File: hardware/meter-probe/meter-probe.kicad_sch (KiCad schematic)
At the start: 29 parts, among them J1 Cable, J2 Cable, Q1 BSS138, SW1 Sensor Button, U1 RT9193, U2 TCS3472, U3 TCA9517A, U4 USBLC6-2SC6, U5 M24C02-D

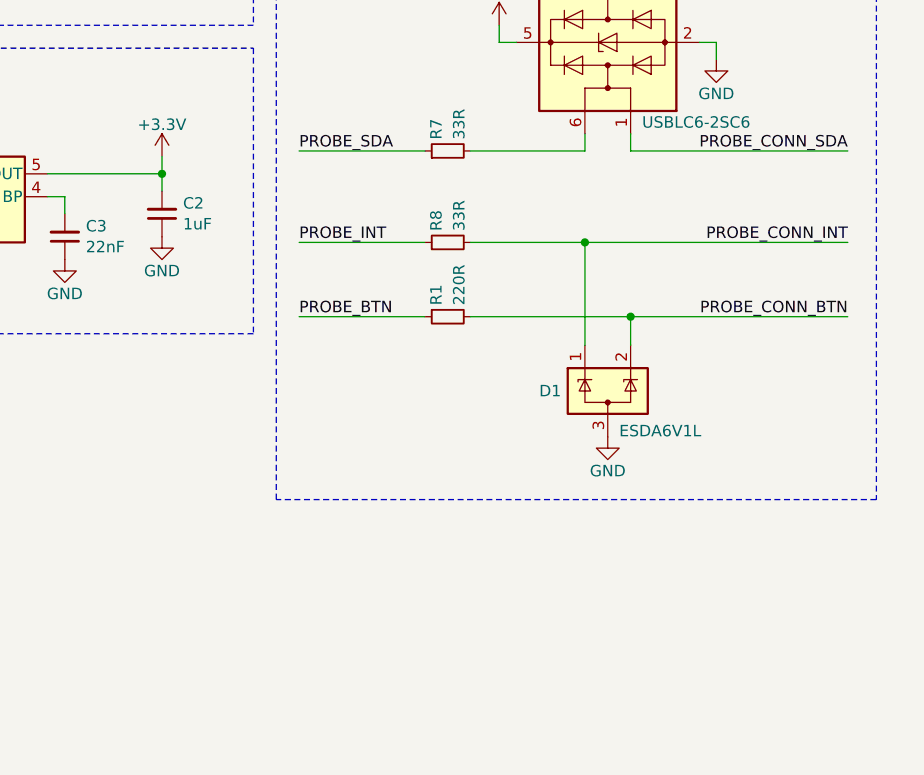
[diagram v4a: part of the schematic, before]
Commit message: Update meter probe PCB layout based on schematic changes
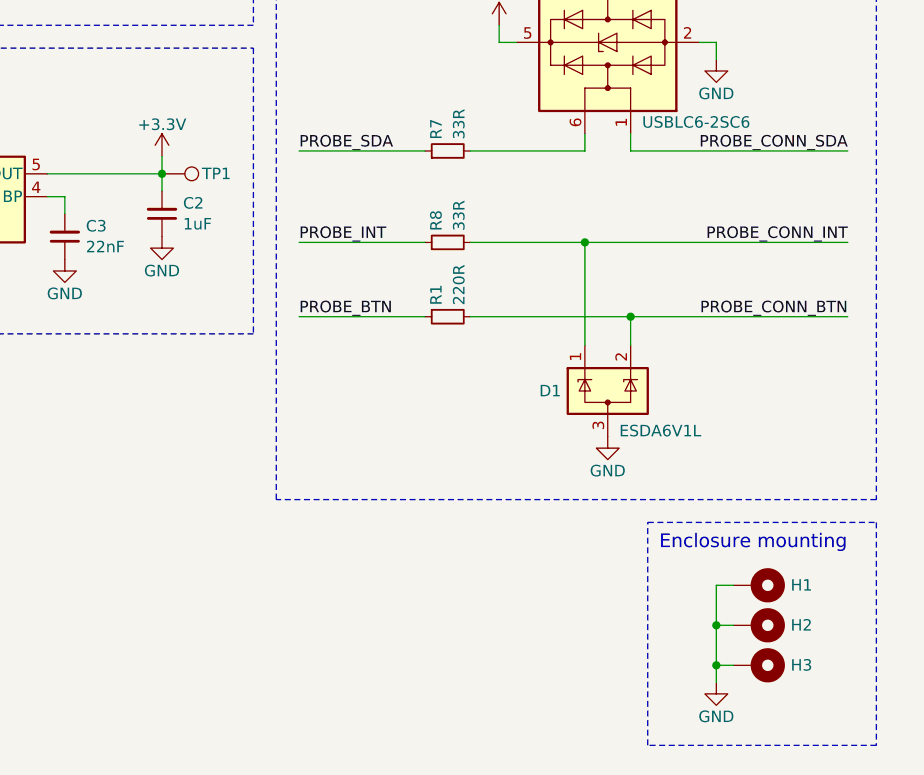
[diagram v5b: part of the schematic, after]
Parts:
- added H1, H2, H3: MountingHole_Pad, MountingHole:MountingHole_2.7mm_M2.5_Pad_Via, symbol Mechanical:MountingHole_Pad
- added TP1: TestPoint, TestPoint:TestPoint_Pad_D2.0mm, symbol Connector:TestPoint
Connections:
- net +3.3V: now also TP1.1
- net GND: now also H1.1, H2.1, H3.1
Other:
- note added: "Enclosure mounting"
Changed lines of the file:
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@@
   (junction (at 125.095 27.305) (diameter 0) (color 0 0 0 0)
   )
+  (junction (at 245.745 148.59) (diameter 0) (color 0 0 0 0)
+  )
   (junction (at 175.26 37.465) (diameter 0) (color 0 0 0 0)
   )
@@
   )
   (junction (at 121.92 41.275) (diameter 0) (color 0 0 0 0)
+  )
+  (junction (at 245.745 153.035) (diameter 0) (color 0 0 0 0)
   )
   (junction (at 168.91 41.275) (diameter 0) (color 0 0 0 0)
@@
     (stroke (width 0) (type default))
   )
+  (wire (pts (xy 245.745 153.035) (xy 245.745 154.94))
+    (stroke (width 0) (type default))
+  )
   (wire (pts (xy 217.805 36.195) (xy 222.885 36.195))
     (stroke (width 0) (type default))
@@
     (stroke (width 0) (type default))
   )
+  (wire (pts (xy 245.745 148.59) (xy 245.745 153.035))
+    (stroke (width 0) (type default))
+  )
   (wire (pts (xy 128.27 27.305) (xy 128.27 28.575))
     (stroke (width 0) (type default))
@@
     (stroke (width 0) (type default))
   )
+  (wire (pts (xy 245.745 153.035) (xy 247.65 153.035))
+    (stroke (width 0) (type default))
+  )
   (wire (pts (xy 199.39 38.735) (xy 222.885 38.735))
     (stroke (width 0) (type default))
@@
     (stroke (width 0) (type default))
   )
+  (wire (pts (xy 245.745 148.59) (xy 247.65 148.59))
+    (stroke (width 0) (type default))
+  )
+  (wire (pts (xy 245.745 144.145) (xy 245.745 148.59))
+    (stroke (width 0) (type default))
+  )
   (wire (pts (xy 125.095 27.305) (xy 128.27 27.305))
     (stroke (width 0) (type default))
@@
   )
   (wire (pts (xy 245.745 83.82) (xy 245.745 85.725))
+    (stroke (width 0) (type default))
+  )
+  (wire (pts (xy 247.65 144.145) (xy 245.745 144.145))
     (stroke (width 0) (type default))
   )
@@
     (fill (type none))
   )
+  (rectangle (start 238.125 137.16) (end 263.525 161.925)
+    (stroke (width 0) (type dash))
+    (fill (type none))
+  )
   (rectangle (start 240.03 17.78) (end 261.62 38.1)
     (stroke (width 0) (type default))
@@
     (at 104.14 80.645 0)
     (effects (font (size 1.27 1.27)) (justify left bottom))
+  )
+  (text "Enclosure mounting" (at 239.395 140.335 0)
+    (effects (font (size 1.524 1.524)) (justify left bottom))
   )
   (text "Red" (at 254 26.67 0)
@@
         (path "/1f1005f7-3f58-4453-9bfa-bdc1c0b6f7ed"
           (reference "#PWR0119") (unit 1)
+        )
+      )
+    )
+  )
+  (symbol (lib_id "Mechanical:MountingHole_Pad") (at 250.19 144.145 270) (unit 1)
+    (in_bom no) (on_board yes) (dnp no)
+    (property "Reference" "H1" (at 254 144.145 90)
+      (effects (font (size 1.27 1.27)) (justify left))
+    )
+    (property "Value" "MountingHole_Pad" (at 254 146.05 90)
+      (effects (font (size 1.27 1.27)) (justify left) hide)
+    )
+    (property "Footprint" "MountingHole:MountingHole_2.7mm_M2.5_Pad_Via" (at 250.19 144.145 0)
+      (effects (font (size 1.27 1.27)) hide)
+    )
+    (property "Datasheet" "~" (at 250.19 144.145 0)
+      (effects (font (size 1.27 1.27)) hide)
+    )
+    (property "Description" "" (at 250.19 144.145 0)
+      (effects (font (size 1.27 1.27)) hide)
+    )
+    (property "Manufacturer" "" (at 250.19 144.145 0)
+      (effects (font (size 1.27 1.27)) hide)
+    )
+    (property "Manufacturer PN" "" (at 250.19 144.145 0)
+      (effects (font (size 1.27 1.27)) hide)
+    )
+    (property "Supplier" "" (at 250.19 144.145 0)
+      (effects (font (size 1.27 1.27)) hide)
+    )
+    (property "Supplier PN" "" (at 250.19 144.145 0)
+      (effects (font (size 1.27 1.27)) hide)
+    )
+    (pin "1")
+    (instances
+      (project "meter-probe"
+        (path "/1f1005f7-3f58-4453-9bfa-bdc1c0b6f7ed"
+          (reference "H1") (unit 1)
         )
       )
@@
     )
   )
+  (symbol (lib_id "power:GND") (at 245.745 154.94 0) (unit 1)
+    (in_bom yes) (on_board yes) (dnp no)
+    (property "Reference" "#PWR016" (at 245.745 161.29 0)
+      (effects (font (size 1.27 1.27)) hide)
+    )
+    (property "Value" "GND" (at 245.745 158.75 0)
+      (effects (font (size 1.27 1.27)))
+    )
+    (property "Footprint" "" (at 245.745 154.94 0)
+      (effects (font (size 1.27 1.27)) hide)
+    )
+    (property "Datasheet" "" (at 245.745 154.94 0)
+      (effects (font (size 1.27 1.27)) hide)
+    )
+    (pin "1")
+    (instances
+      (project "meter-probe"
+        (path "/1f1005f7-3f58-4453-9bfa-bdc1c0b6f7ed"
+          (reference "#PWR016") (unit 1)
+        )
+      )
+      (project "main-board"
+        (path "/31a301d9-d769-4a35-943a-fe3e3609e773/00000000-0000-0000-0000-00005fa19aff"
+          (reference "#PWR072") (unit 1)
+        )
+      )
+    )
+  )
+  (symbol (lib_id "Mechanical:MountingHole_Pad") (at 250.19 153.035 270) (unit 1)
+    (in_bom no) (on_board yes) (dnp no)
+    (property "Reference" "H3" (at 254 153.035 90)
+      (effects (font (size 1.27 1.27)) (justify left))
+    )
+    (property "Value" "MountingHole_Pad" (at 254 154.94 90)
+      (effects (font (size 1.27 1.27)) (justify left) hide)
+    )
+    (property "Footprint" "MountingHole:MountingHole_2.7mm_M2.5_Pad_Via" (at 250.19 153.035 0)
+      (effects (font (size 1.27 1.27)) hide)
+    )
+    (property "Datasheet" "~" (at 250.19 153.035 0)
+      (effects (font (size 1.27 1.27)) hide)
+    )
+    (property "Description" "" (at 250.19 153.035 0)
+      (effects (font (size 1.27 1.27)) hide)
+    )
+    (property "Manufacturer" "" (at 250.19 153.035 0)
+      (effects (font (size 1.27 1.27)) hide)
+    )
+    (property "Manufacturer PN" "" (at 250.19 153.035 0)
+      (effects (font (size 1.27 1.27)) hide)
+    )
+    (property "Supplier" "" (at 250.19 153.035 0)
+      (effects (font (size 1.27 1.27)) hide)
+    )
+    (property "Supplier PN" "" (at 250.19 153.035 0)
+      (effects (font (size 1.27 1.27)) hide)
+    )
+    (pin "1")
+    (instances
+      (project "meter-probe"
+        (path "/1f1005f7-3f58-4453-9bfa-bdc1c0b6f7ed"
+          (reference "H3") (unit 1)
+        )
+      )
+    )
+  )
+  (symbol (lib_id "Connector:TestPoint") (at 184.15 98.425 270) (unit 1)
+    (in_bom no) (on_board yes) (dnp no)
+    (property "Reference" "TP1" (at 188.595 98.425 90)
+      (effects (font (size 1.27 1.27)) (justify left))
+    )
+    (property "Value" "TestPoint" (at 189.23 100.33 90)
+      (effects (font (size 1.27 1.27)) (justify left) hide)
+    )
+    (property "Footprint" "TestPoint:TestPoint_Pad_D2.0mm" (at 184.15 103.505 0)
+      (effects (font (size 1.27 1.27)) hide)
+    )
+    (property "Datasheet" "~" (at 184.15 103.505 0)
+      (effects (font (size 1.27 1.27)) hide)
+    )
+    (property "Description" "" (at 184.15 98.425 0)
+      (effects (font (size 1.27 1.27)) hide)
+    )
+    (property "Manufacturer" "" (at 184.15 98.425 0)
+      (effects (font (size 1.27 1.27)) hide)
+    )
+    (property "Manufacturer PN" "" (at 184.15 98.425 0)
+      (effects (font (size 1.27 1.27)) hide)
+    )
+    (property "Supplier" "" (at 184.15 98.425 0)
+      (effects (font (size 1.27 1.27)) hide)
+    )
+    (property "Supplier PN" "" (at 184.15 98.425 0)
+      (effects (font (size 1.27 1.27)) hide)
+    )
+    (pin "1")
+    (instances
+      (project "meter-probe"
+        (path "/1f1005f7-3f58-4453-9bfa-bdc1c0b6f7ed"
+          (reference "TP1") (unit 1)
+        )
+      )
+    )
+  )
   (symbol (lib_id "Device:C_Small") (at 158.115 29.21 270) (unit 1)
     (in_bom yes) (on_board yes) (dnp no)
@@
         )
       )
+    )
+  )
+  (symbol (lib_id "Mechanical:MountingHole_Pad") (at 250.19 148.59 270) (unit 1)
+    (in_bom no) (on_board yes) (dnp no)
+    (property "Reference" "H2" (at 254 148.59 90)
+      (effects (font (size 1.27 1.27)) (justify left))
+    )
+    (property "Value" "MountingHole_Pad" (at 254 150.495 90)
+      (effects (font (size 1.27 1.27)) (justify left) hide)
+    )
+    (property "Footprint" "MountingHole:MountingHole_2.7mm_M2.5_Pad_Via" (at 250.19 148.59 0)
+      (effects (font (size 1.27 1.27)) hide)
+    )
+    (property "Datasheet" "~" (at 250.19 148.59 0)
+      (effects (font (size 1.27 1.27)) hide)
+    )
+    (property "Description" "" (at 250.19 148.59 0)
+      (effects (font (size 1.27 1.27)) hide)
+    )
+    (property "Manufacturer" "" (at 250.19 148.59 0)
+      (effects (font (size 1.27 1.27)) hide)
+    )
+    (property "Manufacturer PN" "" (at 250.19 148.59 0)
+      (effects (font (size 1.27 1.27)) hide)
+    )
+    (property "Supplier" "" (at 250.19 148.59 0)
+      (effects (font (size 1.27 1.27)) hide)
+    )
+    (property "Supplier PN" "" (at 250.19 148.59 0)
+      (effects (font (size 1.27 1.27)) hide)
+    )
+    (pin "1")
+    (instances
+      (project "meter-probe"
+        (path "/1f1005f7-3f58-4453-9bfa-bdc1c0b6f7ed"
+          (reference "H2") (unit 1)
+        )
+      )

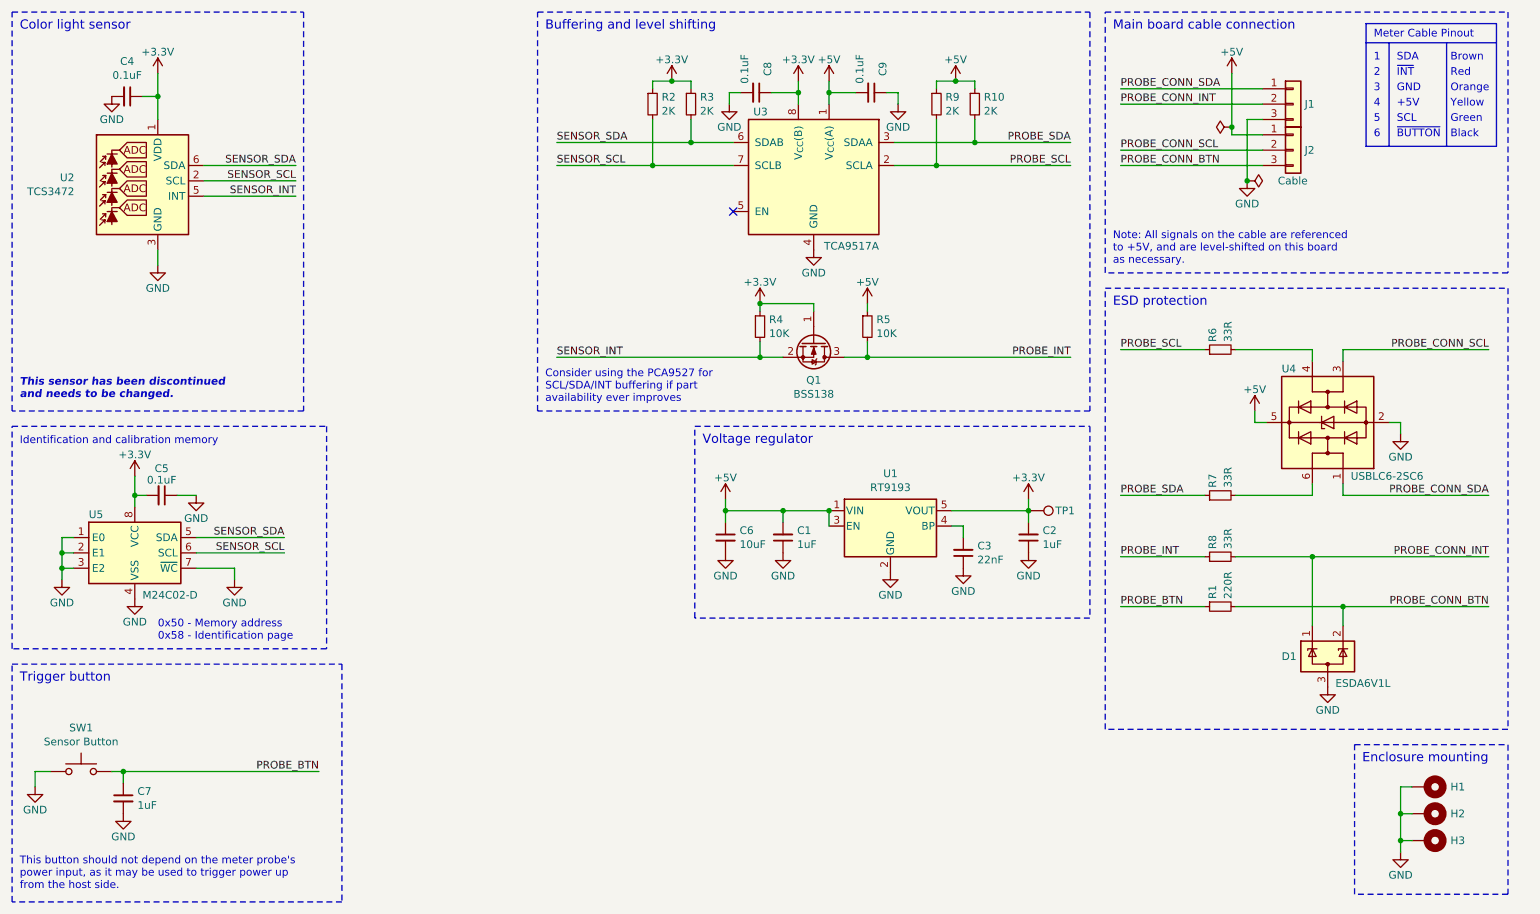
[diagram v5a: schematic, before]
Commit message: Update schematic to include new sensor and required voltage regulator
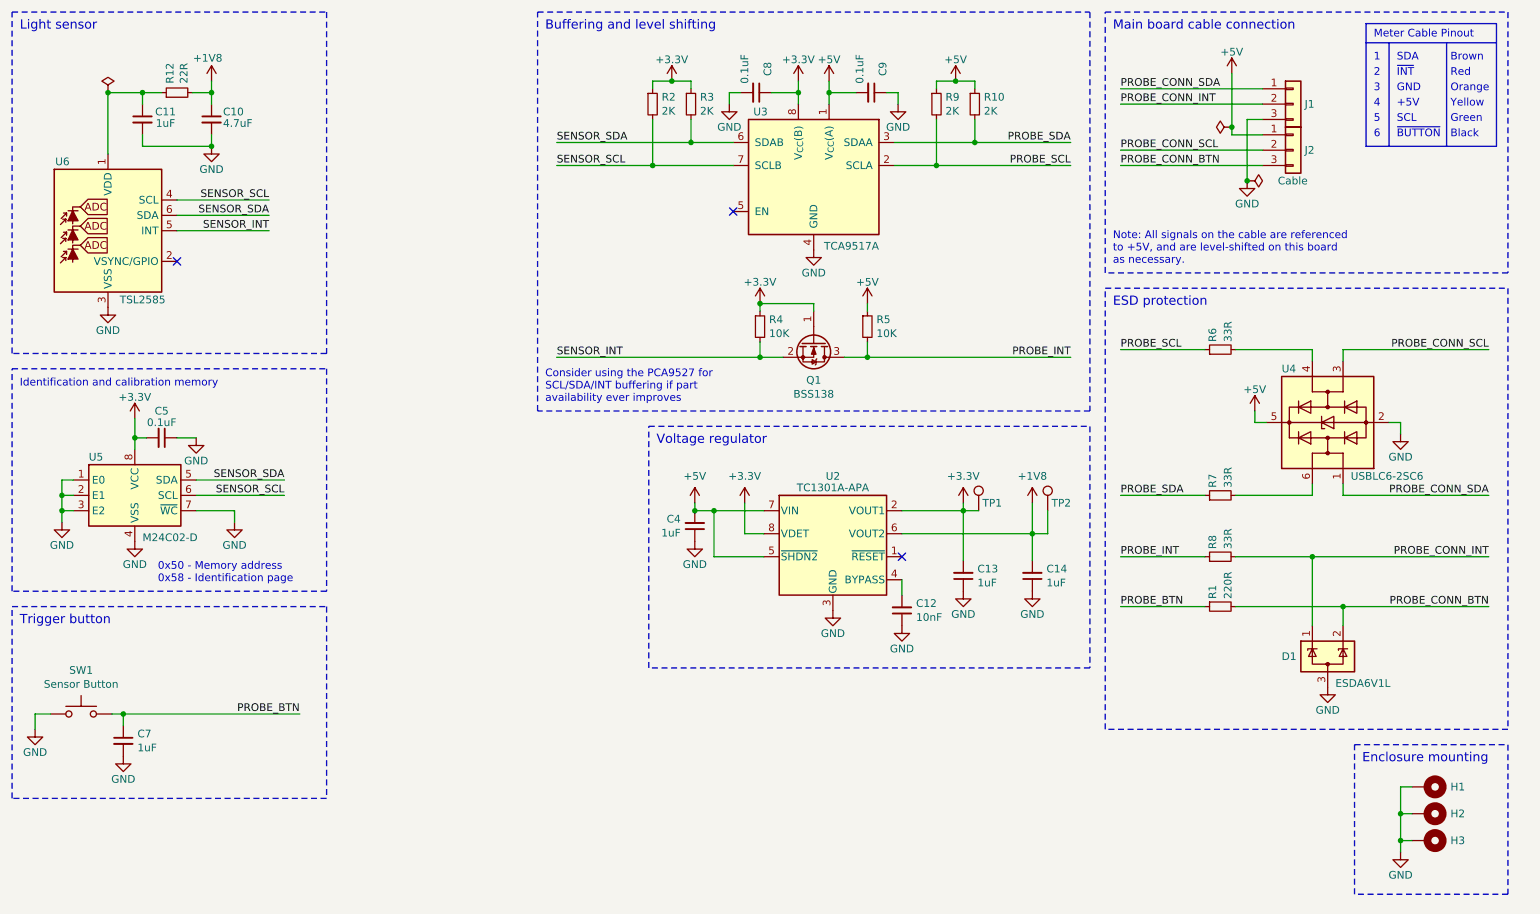
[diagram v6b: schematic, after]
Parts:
- removed C1, C2: 1uF, Capacitor_SMD:C_0603_1608Metric, symbol Device:C_Small
- removed C3: 22nF, Capacitor_SMD:C_0805_2012Metric, symbol Device:C_Small
- removed C6: 10uF, Capacitor_SMD:C_0805_2012Metric, symbol Device:C_Small
- removed U1: RT9193, Package_TO_SOT_SMD:SOT-23-5, symbol Project:RT9193
- removed U2: TCS3472, lib_fp:AMS_TCS3472_DFN-6, symbol Project:TCS3472
- added C10: 4.7uF, Capacitor_SMD:C_0402_1005Metric, symbol Device:C_Small
- added C11: 1uF, Capacitor_SMD:C_0402_1005Metric, symbol Device:C_Small
- added C12: 10nF, Capacitor_SMD:C_0805_2012Metric, symbol Device:C_Small
- added C13, C14: 1uF, Capacitor_SMD:C_0603_1608Metric, symbol Device:C_Small
- added R12: 22R, Resistor_SMD:R_0402_1005Metric, symbol Device:R_Small
- added TP2: 1.8V, TestPoint:TestPoint_Pad_D2.0mm, symbol Connector:TestPoint
- added U2: TC1301A-APA, Package_SO:MSOP-8_3x3mm_P0.65mm, symbol Project:TC1301A
- added U6: TSL2585, lib_fp:AMS_TSL2585_OLGA-6_2x1mm_P0.65mm, symbol Project:TSL2585
- C4: value 0.1uF -> 1uF; Manufacturer PN CL10B104KA8NNNC -> CL10B105KA8NNNC; Supplier Digi-Key -> LCSC; Supplier PN 1276-1006-1-ND -> C29936
- TP1: value TestPoint -> 3.3V; User Label (none) -> 3.3V
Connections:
- net +3.3V: now also C13.2, U2.2 (VOUT1), U2.8 (VDET); no longer C4.1
- net +5V: now also C4.2, U2.5 (~{SHDN2}), U2.7 (VIN)
- net GND: now also C4.1, C10.2, C11.2, C12.1, C13.1, C14.1, U2.3 (GND), U6.3 (VSS); no longer C4.2
- net SENSOR_INT: now also U6.5 (INT)
- net SENSOR_SCL: now also U6.4 (SCL)
- net SENSOR_SDA: now also U6.6 (SDA)
- new net: C11.1, R12.1, U6.1 (VDD)
- new net: C12.2, U2.4 (BYPASS)
- new net +1V8: C10.1, C14.2, R12.2, TP2.1, U2.6 (VOUT2)
- no-connect marks 1 -> 3
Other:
- note added: "Light sensor"
- note removed: "Color light sensor"
- note removed: "This button should not depend on the meter probe's power input, as it may be used to trigger power up from the host side."
- note removed: "This sensor has been discontinued and needs to be changed."
- moved on the sheet: C5, C7, SW1, U5
